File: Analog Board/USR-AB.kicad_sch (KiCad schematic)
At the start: 3 parts, among them U2 CD74HC4067SM96

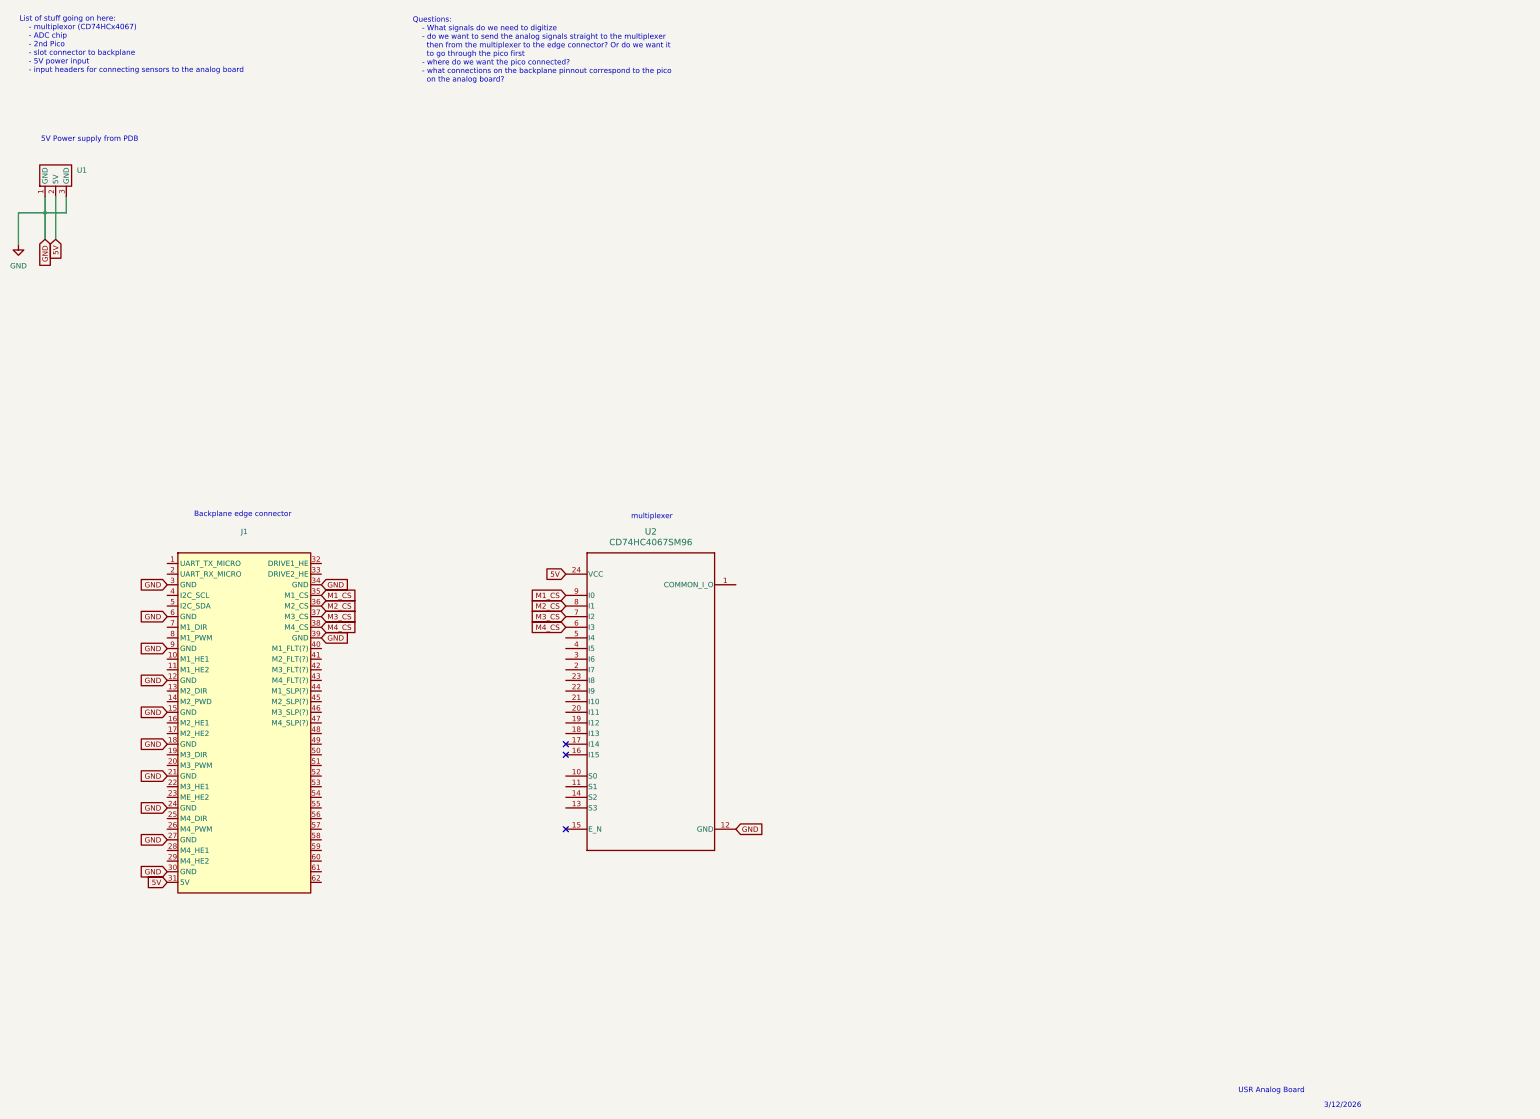
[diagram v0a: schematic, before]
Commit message: Updated Analog Board schem, added comments and pico symbol
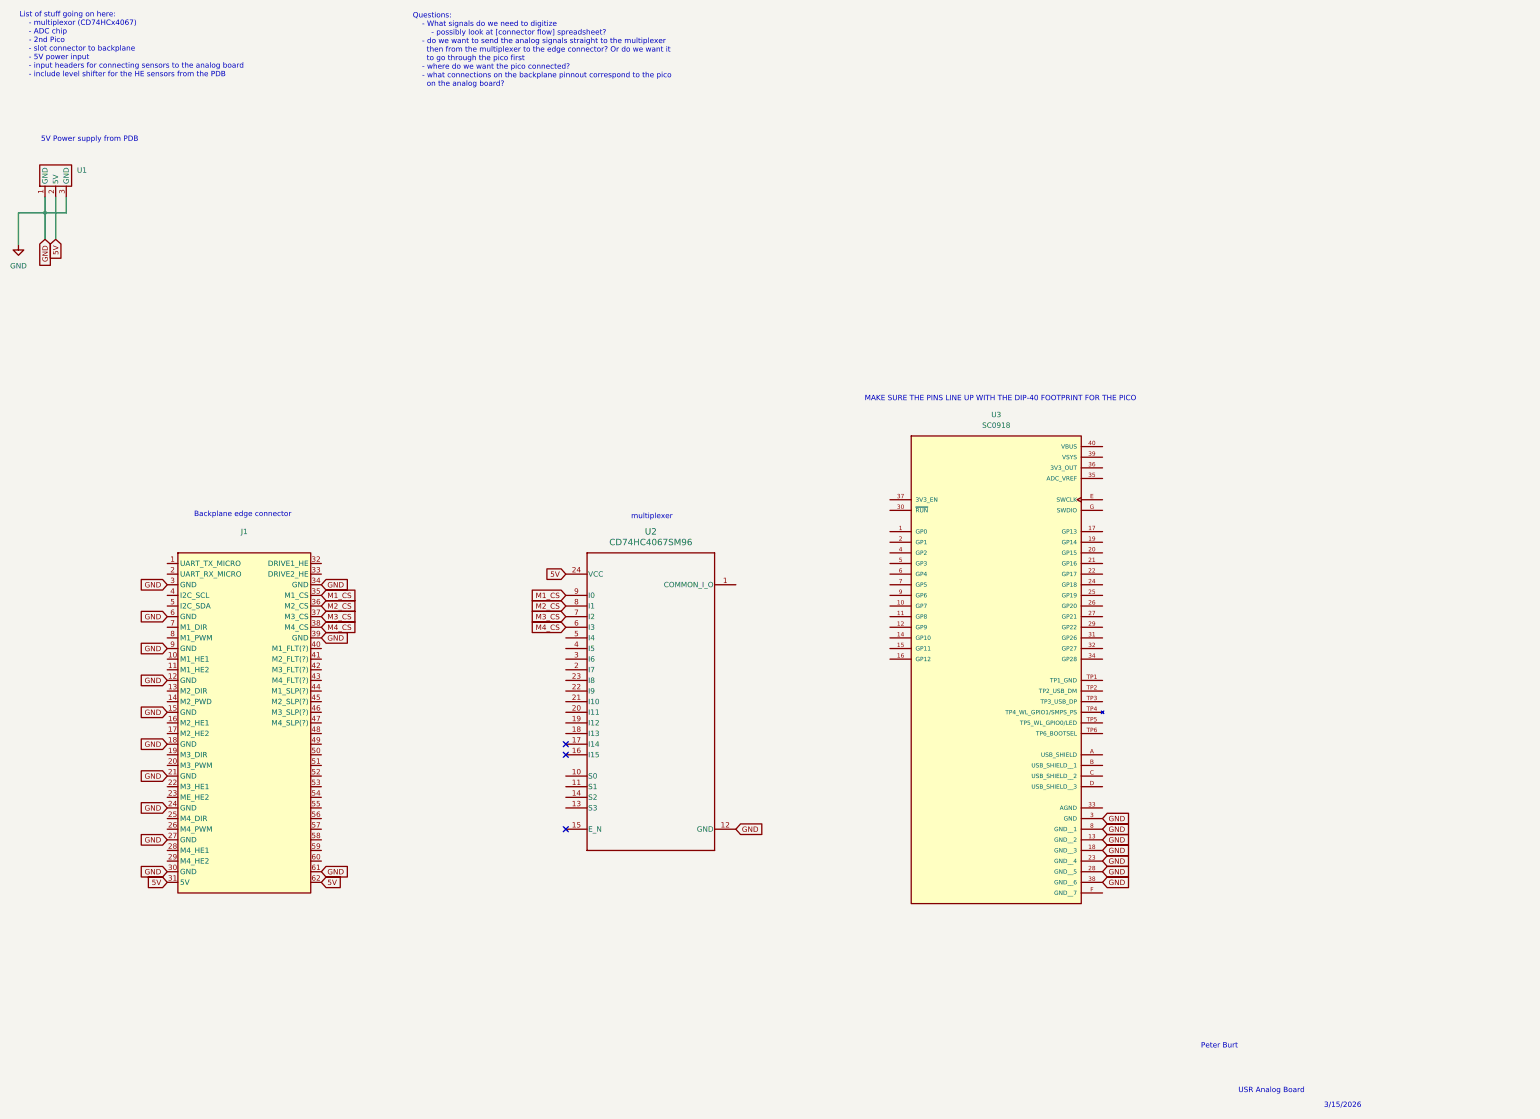
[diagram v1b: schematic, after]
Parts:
- added U3: SC0918, Package_DIP:DIP-40_W15.24mm_LongPads, symbol USR:SC0918
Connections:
- net 5V: now also J1.62
- net GND: now also J1.61, U3.13 (GND__2), U3.18 (GND__3), U3.23 (GND__4), U3.28 (GND__5), U3.3 (GND), U3.38 (GND__6), U3.8 (GND__1)
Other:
- note added: "3/15/2026"
- note added: "List of stuff going on here: - multiplexor (CD74HCx4067) - ADC chip - 2nd Pico - slot connector to backplane - 5V power input - input headers for connecting sensors to the analog board - include level shifter for the HE sensors from the PDB"
- note added: "MAKE SURE THE PINS LINE UP WITH THE DIP-40 FOOTPRINT FOR THE PICO"
- note added: "Peter Burt"
- note added: "Questions: - What signals do we need to digitize - possibly look at [connector flow] spreadsheet? - do we want to send the analog signals straight to the multiplexer then from the multiplexer to the edge connector? Or do we want it to go through the pico first - where do we want the pico connected? - what connections on the backplane pinnout correspond to the pico on the analog board?"
- note removed: "3/12/2026"
- note removed: "List of stuff going on here: - multiplexor (CD74HCx4067) - ADC chip - 2nd Pico - slot connector to backplane - 5V power input - input headers for connecting sensors to the analog board"
- note removed: "Questions: - What signals do we need to digitize - do we want to send the analog signals straight to the multiplexer then from the multiplexer to the edge connector? Or do we want it to go through the pico first - where do we want the pico connected? - what connections on the backplane pinnout correspond to the pico on the analog board?"

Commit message: updated Analog board schematic
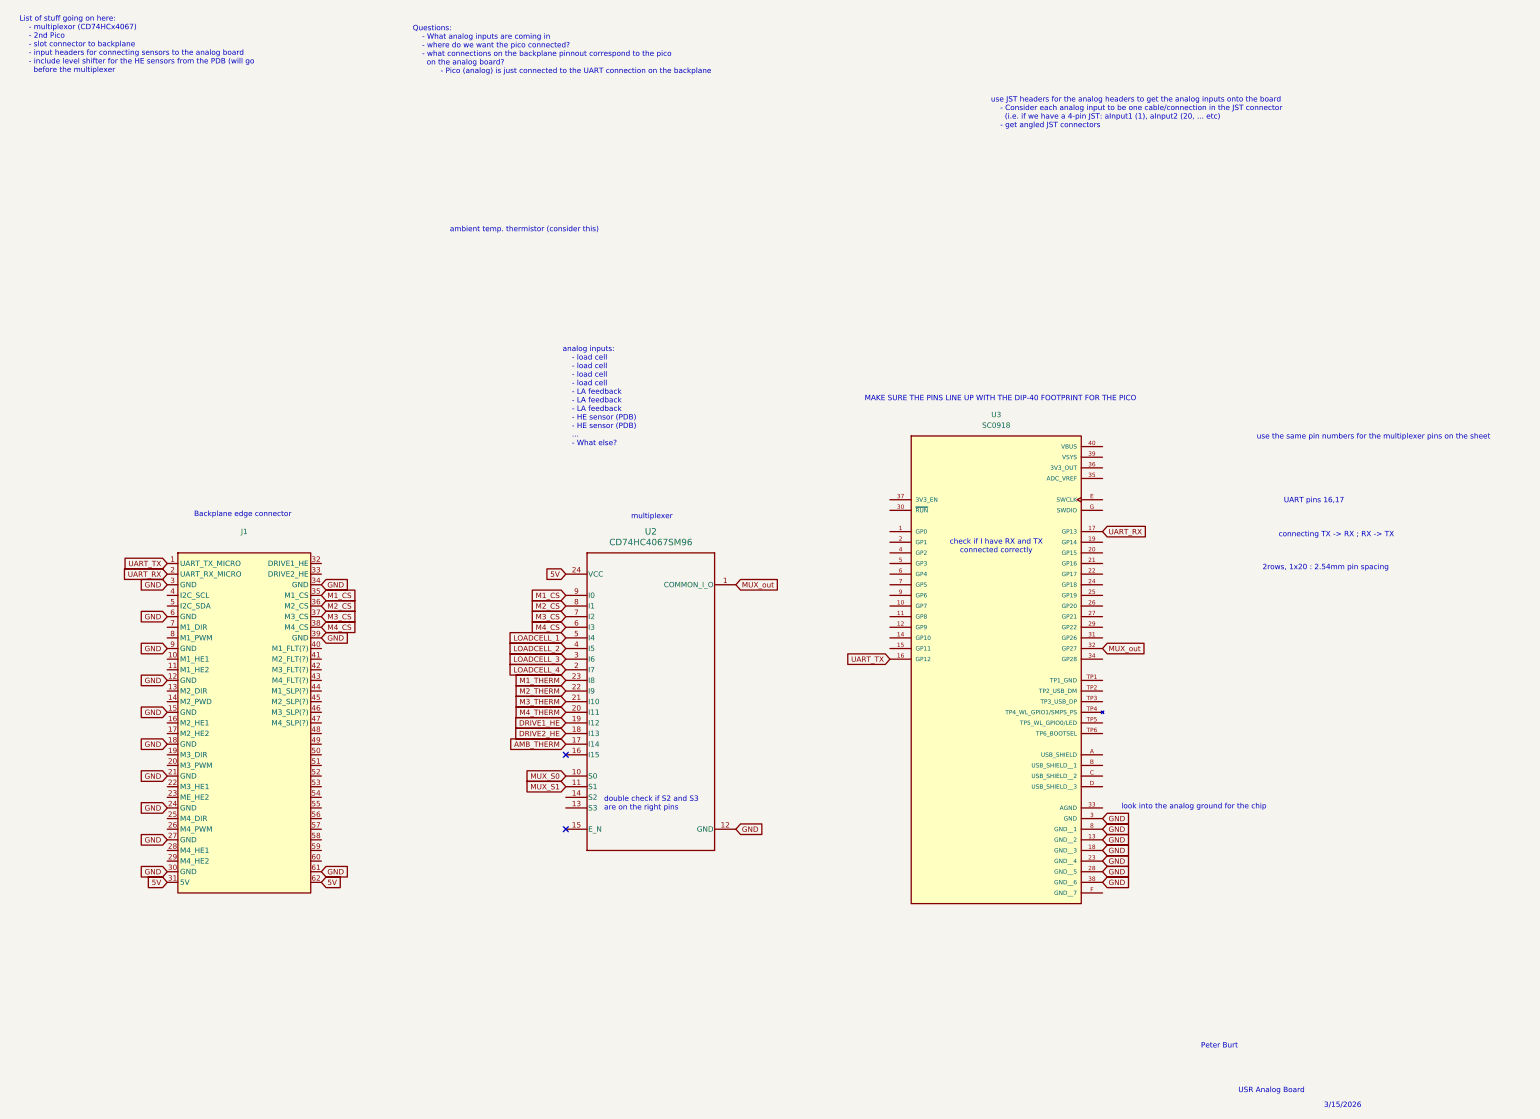
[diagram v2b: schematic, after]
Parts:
- removed U1: ~, USR:JST-XA 3-PIN, symbol USR:JST-XA_3-PIN
- U3: footprint Package_DIP:DIP-40_W15.24mm_LongPads -> Module:RaspberryPi_Pico_Common_THT
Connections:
- net UART_TX: now reaches U3.16 (GP12)
- net UART_TX: now also J1.1 (UART_TX_MICRO)
- net UART_RX: now reaches U3.17 (GP13)
- net UART_RX: now also J1.2 (UART_RX_MICRO)
- net MUX_out: now reaches U3.32 (GP27)
- net MUX_out: now also U2.1 (COMMON_I_O)
- net MUX_S0: now reaches U2.10 (S0)
- net MUX_S1: now reaches U2.11 (S1)
- net AMB_THERM: now reaches U2.17 (I14)
- net DRIVE2_HE: now reaches U2.18 (I13)
- net DRIVE1_HE: now reaches U2.19 (I12)
- net LOADCELL_4: now reaches U2.2 (I7)
- net M4_THERM: now reaches U2.20 (I11)
- net M3_THERM: now reaches U2.21 (I10)
- net M2_THERM: now reaches U2.22 (I9)
- net M1_THERM: now reaches U2.23 (I8)
- net LOADCELL_3: now reaches U2.3 (I6)
- net LOADCELL_2: now reaches U2.4 (I5)
- net LOADCELL_1: now reaches U2.5 (I4)
- no-connect marks 3 -> 2
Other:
- note added: "2rows, 1x20 : 2.54mm pin spacing"
- note added: "List of stuff going on here: - multiplexor (CD74HCx4067) - 2nd Pico - slot connector to backplane - input headers for connecting sensors to the analog board - include level shifter for the HE sensors from the PDB (will go before the multiplexer"
- note added: "Questions: - What analog inputs are coming in - where do we want the pico connected? - what connections on the backplane pinnout correspond to the pico on the analog board? - Pico (analog) is just connected to the UART connection on the backplane"
- note added: "UART pins 16,17"
- note added: "ambient temp. thermistor (consider this)"
- note added: "analog inputs: - load cell - load cell - load cell - load cell - LA feedback - LA feedback - LA feedback - HE sensor (PDB) - HE sensor (PDB) ... - What else?"
- note added: "check if I have RX and TX connected correctly"
- note added: "connecting TX -> RX ; RX -> TX"
- note added: "double check if S2 and S3 are on the right pins"
- note added: "look into the analog ground for the chip"
- note added: "use JST headers for the analog headers to get the analog inputs onto the board - Consider each analog input to be one cable/connection in the JST connector (i.e. if we have a 4-pin JST: aInput1 (1), aInput2 (20, ... etc) - get angled JST connectors"
- note added: "use the same pin numbers for the multiplexer pins on the sheet"
- note removed: "5V Power supply from PDB"
- note removed: "List of stuff going on here: - multiplexor (CD74HCx4067) - ADC chip - 2nd Pico - slot connector to backplane - 5V power input - input headers for connecting sensors to the analog board - include level shifter for the HE sensors from the PDB"
- note removed: "Questions: - What signals do we need to digitize - possibly look at [connector flow] spreadsheet? - do we want to send the analog signals straight to the multiplexer then from the multiplexer to the edge connector? Or do we want it to go through the pico first - where do we want the pico connected? - what connections on the backplane pinnout correspond to the pico on the analog board?"

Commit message: Updated analog board routing
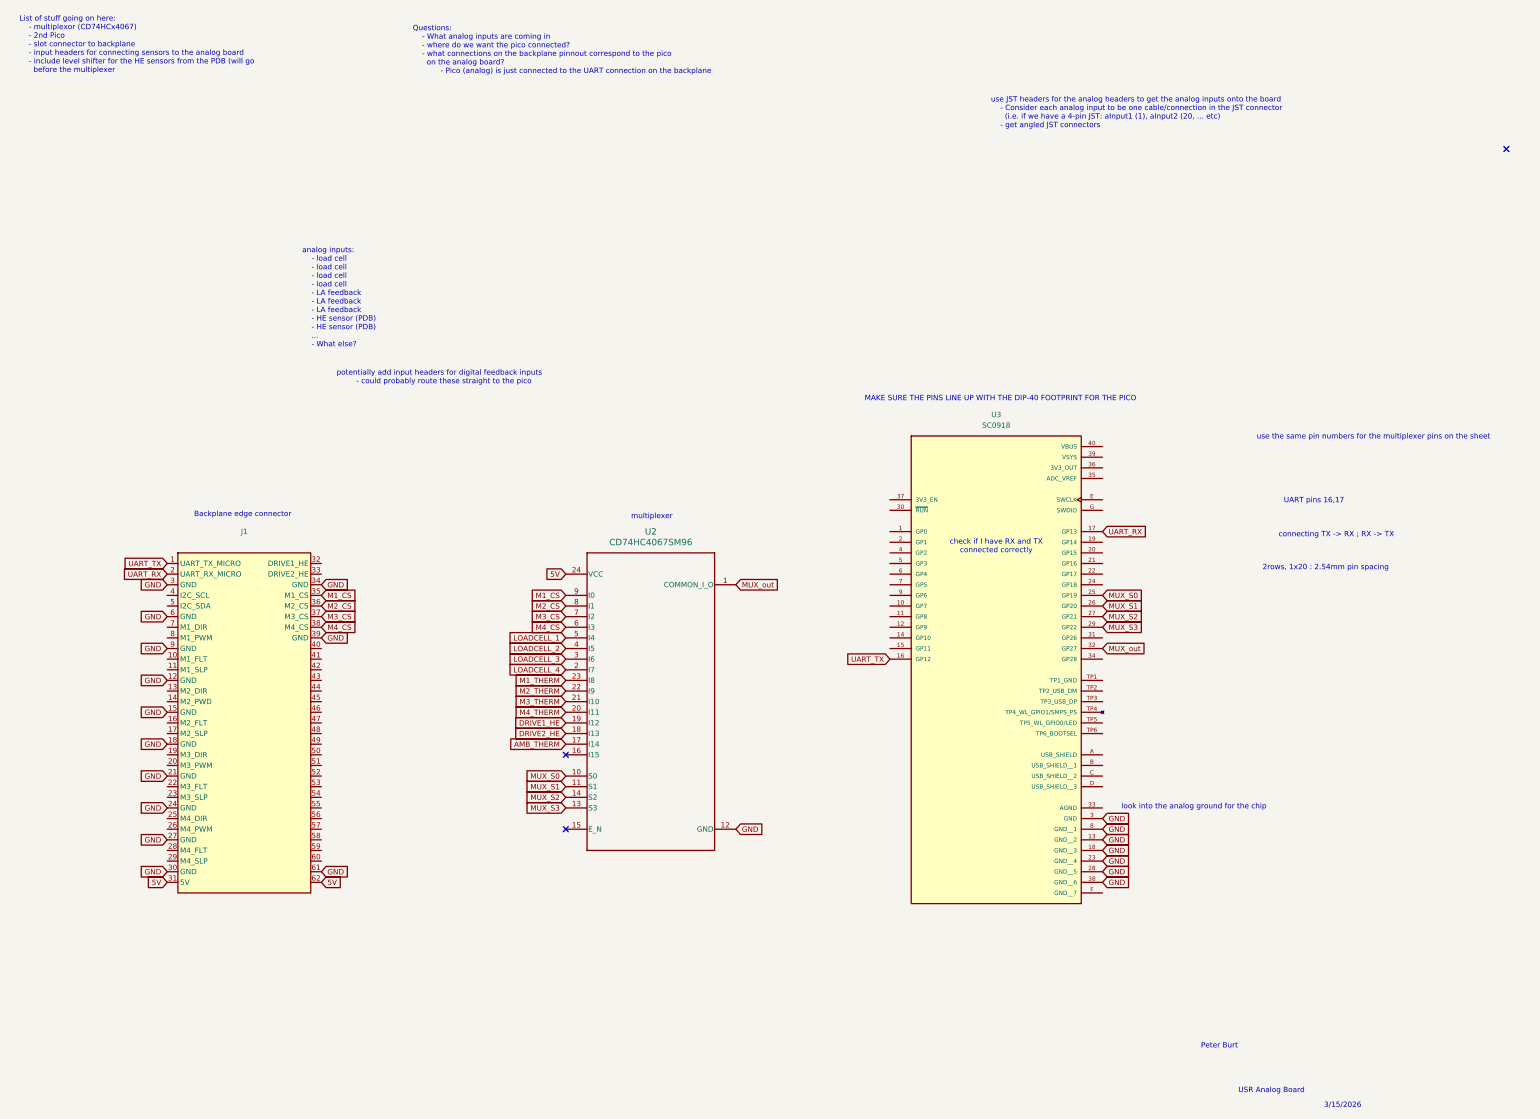
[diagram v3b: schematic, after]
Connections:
- net MUX_S0: now also U3.25 (GP19)
- net MUX_S1: now also U3.26 (GP20)
- net MUX_S2: now reaches U3.27 (GP21)
- net MUX_S2: now also U2.14 (S2)
- net MUX_S3: now reaches U3.29 (GP22)
- net MUX_S3: now also U2.13 (S3)
- no-connect marks 2 -> 3
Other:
- note added: "potentially add input headers for digital feedback inputs - could probably route these straight to the pico"
- note removed: "ambient temp. thermistor (consider this)"
- note removed: "double check if S2 and S3 are on the right pins"
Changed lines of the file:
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@@
+		)
+	)
+	(text "potentially add input headers for digital feedback inputs \n	- could probably route these straight to the pico"
+		(exclude_from_sim no)
+		(at 119.634 106.68 0)
+		(effects
+			(font
+				(size 1.27 1.27)
+			)
 		)
 	)
 	(text "analog inputs:\n	- load cell\n	- load cell\n	- load cell\n	- load cell\n	- LA feedback\n	- LA feedback\n	- LA feedback\n	- HE sensor (PDB)\n	- HE sensor (PDB)\n	...\n	- What else?"
 		(exclude_from_sim no)
-		(at 149.098 111.252 0)
-		(effects
-			(font
-				(size 1.27 1.27)
-			)
-			(justify left)
-		)
-	)
-	(text "ambient temp. thermistor (consider this)"
-		(exclude_from_sim no)
-		(at 139.954 71.374 0)
-		(effects
-			(font
-				(size 1.27 1.27)
-			)
+		(at 86.868 87.63 0)
+		(effects
+			(font
+				(size 1.27 1.27)
+			)
+			(justify left)
 		)
 	)
@@
 		)
 	)
-	(text "double check if S2 and S3 \nare on the right pins\n"
-		(exclude_from_sim no)
-		(at 159.004 208.534 0)
-		(effects
-			(font
-				(size 1.27 1.27)
-			)
-			(justify left)
-		)
-	)
 	(text "USR Analog Board"
 		(exclude_from_sim no)
@@
 		(at 149.86 214.63)
 	)
+	(no_connect
+		(at 374.65 52.07)
+	)
 	(global_label "M3_CS"
 		(shape input)
@@
 		)
 	)
+	(global_label "MUX_S1"
+		(shape input)
+		(at 278.13 161.29 0)
+		(fields_autoplaced yes)
+		(effects
+			(font
+				(size 1.27 1.27)
+			)
+			(justify left)
+		)
+		(property "Intersheetrefs" "${INTERSHEET_REFS}"
+			(at 288.4932 161.29 0)
+			(effects
+				(font
+					(size 1.27 1.27)
+				)
+				(justify left)
+				(hide yes)
+			)
+		)
+	)
 	(global_label "GND"
 		(shape input)
@@
 		)
 	)
+	(global_label "MUX_S3"
+		(shape input)
+		(at 149.86 209.55 180)
+		(fields_autoplaced yes)
+		(effects
+			(font
+				(size 1.27 1.27)
+			)
+			(justify right)
+		)
+		(property "Intersheetrefs" "${INTERSHEET_REFS}"
+			(at 139.4968 209.55 0)
+			(effects
+				(font
+					(size 1.27 1.27)
+				)
+				(justify right)
+				(hide yes)
+			)
+		)
+	)
+	(global_label "MUX_S0"
+		(shape input)
+		(at 278.13 158.75 0)
+		(fields_autoplaced yes)
+		(effects
+			(font
+				(size 1.27 1.27)
+			)
+			(justify left)
+		)
+		(property "Intersheetrefs" "${INTERSHEET_REFS}"
+			(at 288.4932 158.75 0)
+			(effects
+				(font
+					(size 1.27 1.27)
+				)
+				(justify left)
+				(hide yes)
+			)
+		)
+	)
+	(global_label "MUX_S2"
+		(shape input)
+		(at 149.86 207.01 180)
+		(fields_autoplaced yes)
+		(effects
+			(font
+				(size 1.27 1.27)
+			)
+			(justify right)
+		)
+		(property "Intersheetrefs" "${INTERSHEET_REFS}"
+			(at 139.4968 207.01 0)
+			(effects
+				(font
+					(size 1.27 1.27)
+				)
+				(justify right)
+				(hide yes)
+			)
+		)
+	)
 	(global_label "GND"
 		(shape input)
@@
 		)
 	)
+	(global_label "MUX_S3"
+		(shape input)
+		(at 278.13 166.37 0)
+		(fields_autoplaced yes)
+		(effects
+			(font
+				(size 1.27 1.27)
+			)
+			(justify left)
+		)
+		(property "Intersheetrefs" "${INTERSHEET_REFS}"
+			(at 288.4932 166.37 0)
+			(effects
+				(font
+					(size 1.27 1.27)
+				)
+				(justify left)
+				(hide yes)
+			)
+		)
+	)
 	(global_label "GND"
 		(shape input)
@@
 				(hide yes)
 			)
+		)
+	)
+	(global_label "MUX_S2"
+		(shape input)
+		(at 278.13 163.83 0)
+		(fields_autoplaced yes)
+		(effects
+			(font
+				(size 1.27 1.27)
+			)
+			(justify left)
+		)
+		(property "Intersheetrefs" "${INTERSHEET_REFS}"
+			(at 288.4932 163.83 0)
+			(effects
+				(font
+					(size 1.27 1.27)
+				)
+				(justify left)
+				(hide yes)
+			)
